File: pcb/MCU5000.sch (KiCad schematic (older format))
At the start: 10 parts, among them J16 Conn_01x04_Female, J17 Conn_01x04_Female, J18 Conn_01x04_Female

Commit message: Nice labels
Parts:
- R15, R16: value 1M -> 2K2
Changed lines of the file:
@@
 P 5850 4550
 F 0 "R15" V 5643 4550 50  0000 C CNN
-F 1 "1M" V 5734 4550 50  0000 C CNN
+F 1 "2K2" V 5734 4550 50  0000 C CNN
 F 2 "Resistor_SMD:R_0603_1608Metric_Pad0.98x0.95mm_HandSolder" V 5780 4550 50  0001 C CNN
 F 3 "~" H 5850 4550 50  0001 C CNN
@@
 P 6250 4900
 F 0 "R16" H 6180 4854 50  0000 R CNN
-F 1 "1M" H 6180 4945 50  0000 R CNN
+F 1 "2K2" H 6180 4945 50  0000 R CNN
 F 2 "Resistor_SMD:R_0603_1608Metric_Pad0.98x0.95mm_HandSolder" V 6180 4900 50  0001 C CNN
 F 3 "~" H 6250 4900 50  0001 C CNN

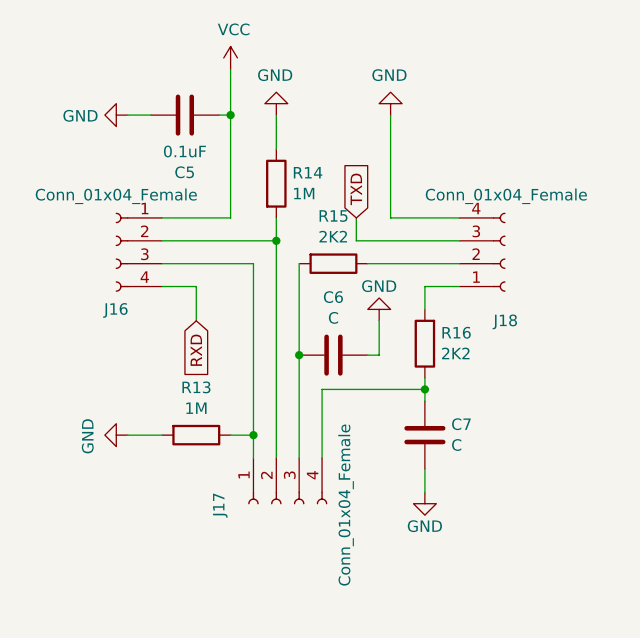
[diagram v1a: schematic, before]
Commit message: Added buzzer
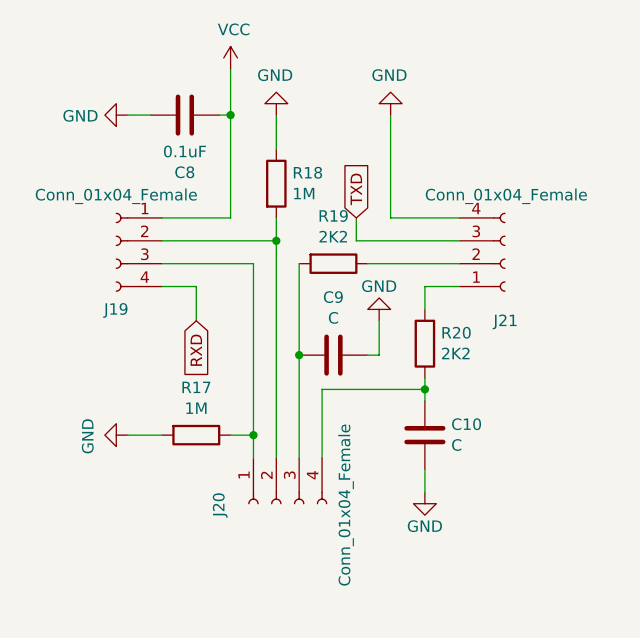
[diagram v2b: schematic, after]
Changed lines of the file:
@@
 $Descr A4 11693 8268
 encoding utf-8
-Sheet 10 10
+Sheet 10 12
 Title ""
 Date ""
@@
 AR Path="/60308700/60350349" Ref="#PWR?"  Part="1"
 AR Path="/6034DF24/60350349" Ref="#PWR013"  Part="1"
-F 0 "#PWR013" H 5400 3550 50  0001 C CNN
+AR Path="/603599D1/60350349" Ref="#PWR0108"  Part="1"
+F 0 "#PWR0108" H 5400 3550 50  0001 C CNN
 F 1 "VCC" H 5415 3873 50  0000 C CNN
 F 2 "" H 5400 3700 50  0001 C CNN
@@
 AR Path="/60308700/6035034F" Ref="#PWR?"  Part="1"
 AR Path="/6034DF24/6035034F" Ref="#PWR011"  Part="1"
-F 0 "#PWR011" H 4950 3650 50  0001 C CNN
+AR Path="/603599D1/6035034F" Ref="#PWR0109"  Part="1"
+F 0 "#PWR0109" H 4950 3650 50  0001 C CNN
 F 1 "GND" V 4955 3772 50  0000 R CNN
 F 2 "" H 4950 3900 50  0001 C CNN
@@
 AR Path="/60308700/60350355" Ref="C?"  Part="1"
 AR Path="/6034DF24/60350355" Ref="C5"  Part="1"
-F 0 "C5" V 4948 3900 50  0000 C CNN
+AR Path="/603599D1/60350355" Ref="C8"  Part="1"
+F 0 "C8" V 4948 3900 50  0000 C CNN
 F 1 "0.1uF" V 5039 3900 50  0000 C CNN
 F 2 "Capacitor_SMD:C_0603_1608Metric_Pad1.08x0.95mm_HandSolder" H 5238 3750 50  0001 C CNN
@@
 AR Path="/60308700/60350361" Ref="#PWR?"  Part="1"
 AR Path="/6034DF24/60350361" Ref="#PWR016"  Part="1"
-F 0 "#PWR016" H 6100 3650 50  0001 C CNN
+AR Path="/603599D1/60350361" Ref="#PWR0110"  Part="1"
+F 0 "#PWR0110" H 6100 3650 50  0001 C CNN
 F 1 "GND" H 6105 3727 50  0000 C CNN
 F 2 "" H 6100 3900 50  0001 C CNN
@@
 AR Path="/60308700/60350368" Ref="J?"  Part="1"
 AR Path="/6034DF24/60350368" Ref="J18"  Part="1"
-F 0 "J18" H 6550 4800 50  0000 L CNN
+AR Path="/603599D1/60350368" Ref="J21"  Part="1"
+F 0 "J21" H 6550 4800 50  0000 L CNN
 F 1 "Conn_01x04_Female" H 6250 4250 50  0000 L CNN
 F 2 "Connector_PinSocket_2.54mm:PinSocket_1x04_P2.54mm_Vertical" H 6600 4550 50  0001 C CNN
@@
 AR Path="/60308700/60350370" Ref="J?"  Part="1"
 AR Path="/6034DF24/60350370" Ref="J16"  Part="1"
-F 0 "J16" H 4900 4150 50  0000 C CNN
+AR Path="/603599D1/60350370" Ref="J19"  Part="1"
+F 0 "J19" H 4900 4150 50  0000 C CNN
 F 1 "Conn_01x04_Female" H 4900 4650 50  0000 C CNN
 F 2 "Connector_PinSocket_2.54mm:PinSocket_1x04_P2.54mm_Vertical" H 4900 4450 50  0001 C CNN
@@
 AR Path="/60308700/60354EB8" Ref="J?"  Part="1"
 AR Path="/6034DF24/60354EB8" Ref="J17"  Part="1"
-F 0 "J17" H 5550 5850 50  0000 L CNN
+AR Path="/603599D1/60354EB8" Ref="J20"  Part="1"
+F 0 "J20" H 5550 5850 50  0000 L CNN
 F 1 "Conn_01x04_Female" H 5250 5300 50  0000 L CNN
 F 2 "Connector_PinSocket_2.54mm:PinSocket_1x04_P2.54mm_Vertical" H 5600 5600 50  0001 C CNN
@@
 U 1 1 603553A1
 P 5600 4200
-F 0 "R14" H 5670 4246 50  0000 L CNN
+AR Path="/6034DF24/603553A1" Ref="R14"  Part="1"
+AR Path="/603599D1/603553A1" Ref="R18"  Part="1"
+F 0 "R18" H 5670 4246 50  0000 L CNN
 F 1 "1M" H 5670 4155 50  0000 L CNN
 F 2 "Resistor_SMD:R_0603_1608Metric_Pad0.98x0.95mm_HandSolder" V 5530 4200 50  0001 C CNN
@@
 AR Path="/60308700/60355E43" Ref="#PWR?"  Part="1"
 AR Path="/6034DF24/60355E43" Ref="#PWR014"  Part="1"
-F 0 "#PWR014" H 5600 3650 50  0001 C CNN
+AR Path="/603599D1/60355E43" Ref="#PWR0111"  Part="1"
+F 0 "#PWR0111" H 5600 3650 50  0001 C CNN
 F 1 "GND" H 5605 3727 50  0000 C CNN
 F 2 "" H 5600 3900 50  0001 C CNN
@@
 U 1 1 603567F0
 P 5250 5300
-F 0 "R13" V 5043 5300 50  0000 C CNN
+AR Path="/6034DF24/603567F0" Ref="R13"  Part="1"
+AR Path="/603599D1/603567F0" Ref="R17"  Part="1"
+F 0 "R17" V 5043 5300 50  0000 C CNN
 F 1 "1M" V 5134 5300 50  0000 C CNN
 F 2 "Resistor_SMD:R_0603_1608Metric_Pad0.98x0.95mm_HandSolder" V 5180 5300 50  0001 C CNN
@@
 AR Path="/60308700/6035723E" Ref="#PWR?"  Part="1"
 AR Path="/6034DF24/6035723E" Ref="#PWR012"  Part="1"
-F 0 "#PWR012" H 4950 5050 50  0001 C CNN
+AR Path="/603599D1/6035723E" Ref="#PWR0112"  Part="1"
+F 0 "#PWR0112" H 4950 5050 50  0001 C CNN
 F 1 "GND" H 4955 5127 50  0000 C CNN
 F 2 "" H 4950 5300 50  0001 C CNN
@@
 U 1 1 60358F4E
 P 5850 4950
-F 0 "C6" V 5598 4950 50  0000 C CNN
+AR Path="/6034DF24/60358F4E" Ref="C6"  Part="1"
+AR Path="/603599D1/60358F4E" Ref="C9"  Part="1"
+F 0 "C9" V 5598 4950 50  0000 C CNN
 F 1 "C" V 5689 4950 50  0000 C CNN
 F 2 "Capacitor_SMD:C_0603_1608Metric_Pad1.08x0.95mm_HandSolder" H 5888 4800 50  0001 C CNN
@@
 U 1 1 6035BBD0
 P 5850 4550
-F 0 "R15" V 5643 4550 50  0000 C CNN
+AR Path="/6034DF24/6035BBD0" Ref="R15"  Part="1"
+AR Path="/603599D1/6035BBD0" Ref="R19"  Part="1"
+F 0 "R19" V 5643 4550 50  0000 C CNN
 F 1 "2K2" V 5734 4550 50  0000 C CNN
 F 2 "Resistor_SMD:R_0603_1608Metric_Pad0.98x0.95mm_HandSolder" V 5780 4550 50  0001 C CNN
@@
 AR Path="/60308700/6035DD5C" Ref="#PWR?"  Part="1"
 AR Path="/6034DF24/6035DD5C" Ref="#PWR015"  Part="1"
-F 0 "#PWR015" H 6050 4550 50  0001 C CNN
+AR Path="/603599D1/6035DD5C" Ref="#PWR0113"  Part="1"
+F 0 "#PWR0113" H 6050 4550 50  0001 C CNN
 F 1 "GND" H 6050 4650 50  0000 C CNN
 F 2 "" H 6050 4800 50  0001 C CNN
@@
 U 1 1 60361E47
 P 6250 4900
-F 0 "R16" H 6180 4854 50  0000 R CNN
+AR Path="/6034DF24/60361E47" Ref="R16"  Part="1"
+AR Path="/603599D1/60361E47" Ref="R20"  Part="1"
+F 0 "R20" H 6180 4854 50  0000 R CNN
 F 1 "2K2" H 6180 4945 50  0000 R CNN
 F 2 "Resistor_SMD:R_0603_1608Metric_Pad0.98x0.95mm_HandSolder" V 6180 4900 50  0001 C CNN
@@
 U 1 1 603636E1
 P 6250 5300
-F 0 "C7" H 6135 5254 50  0000 R CNN
+AR Path="/6034DF24/603636E1" Ref="C7"  Part="1"
+AR Path="/603599D1/603636E1" Ref="C10"  Part="1"
+F 0 "C10" H 6135 5254 50  0000 R CNN
 F 1 "C" H 6135 5345 50  0000 R CNN
 F 2 "Capacitor_SMD:C_0603_1608Metric_Pad1.08x0.95mm_HandSolder" H 6288 5150 50  0001 C CNN
@@
 AR Path="/60308700/60364D99" Ref="#PWR?"  Part="1"
 AR Path="/6034DF24/60364D99" Ref="#PWR017"  Part="1"
-F 0 "#PWR017" H 6250 5300 50  0001 C CNN
+AR Path="/603599D1/60364D99" Ref="#PWR0114"  Part="1"
+F 0 "#PWR0114" H 6250 5300 50  0001 C CNN
 F 1 "GND" H 6250 5400 50  0000 C CNN
 F 2 "" H 6250 5550 50  0001 C CNN

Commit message: Added switches
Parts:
- C6, C7: value C -> 0.1uF
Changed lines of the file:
@@
 $Descr A4 11693 8268
 encoding utf-8
-Sheet 11 13
+Sheet 11 15
 Title ""
 Date ""
@@
 AR Path="/603599D1/60358F4E" Ref="C9"  Part="1"
 F 0 "C9" V 5598 4950 50  0000 C CNN
-F 1 "C" V 5689 4950 50  0000 C CNN
+F 1 "0.1uF" V 5689 4950 50  0000 C CNN
 F 2 "Capacitor_SMD:C_0603_1608Metric_Pad1.08x0.95mm_HandSolder" H 5888 4800 50  0001 C CNN
 F 3 "~" H 5850 4950 50  0001 C CNN
@@
 AR Path="/603599D1/603636E1" Ref="C10"  Part="1"
 F 0 "C10" H 6135 5254 50  0000 R CNN
-F 1 "C" H 6135 5345 50  0000 R CNN
+F 1 "0.1uF" H 6135 5345 50  0000 R CNN
 F 2 "Capacitor_SMD:C_0603_1608Metric_Pad1.08x0.95mm_HandSolder" H 6288 5150 50  0001 C CNN
 F 3 "~" H 6250 5300 50  0001 C CNN
